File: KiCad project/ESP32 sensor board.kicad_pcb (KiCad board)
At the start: 4 copper layers, 104.8 x 50 mm, 82 parts, among them J1 USB_C_Receptacle, J2 JST_2mm_LiPo, J3 GSD090012SEU, J5 B4B-XH-AM__LF__SN_, J6 Conn_01x05, Q1 TEMT6000X01, Q2 BC817, Q3 BC817, SW1 SMD_6x3.5mm_h2.5mm, SW2 SMD_6x3.5mm_h2.5mm, U1 MCP73871, U2 AMS1117-3.3, U3 ESP32-C3-WROOM-02-H4, U4 CP2102N-A02-GQFN20, U5 USBLC6-2SC6, U6 W25Q32JVSSIQ, U7 BME280, U8 MAX4466EXK

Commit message: Replaced the button, USB, bat connector with new symbols and footprints. Completed draft layout and routing.
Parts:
- removed J5: B4B-XH-AM__LF__SN_, Project_Library:JST_B4B-XH-AM__LF__SN_
- added J4: B4B-XH-AM, Project_Library:JST_B4B-XH-AM__LF__SN_, F.Cu at (164.0, 113.8)
- C16, C18, C20: value 100n -> 0.1u
- F1: footprint Project_Library:1210 -> Fuse:Fuse_1210_3225Metric
- R4: value 5K1 -> 5k1
- SW1, SW2: value SMD_6x3.5mm_h2.5mm -> 1101NE; footprint Button_Switch_THT:SW_PUSH_6mm -> Footprints:SW4-SMD-5.2X5.2X1.5MM
- U2: value AMS1117-3.3 -> LM1117MPX-3.3_NOPB; footprint Package_TO_SOT_SMD:SOT-223-3_TabPin2 -> Footprints:VREG_LM1117MPX-3.3_NOPB
- U3: footprint Project_Library:MODULE_ESP32-C3-WROOM-02-H4 -> Footprints:MODULE_ESP32-C3-WROOM-02-H4
- U8: value MAX4466EXK -> MAX4466EXK+T
- moved SW1 4.03 mm to (197.6, 79.7), turned to 180 degrees
- moved SW2 2.88 mm to (197.5, 113.9), turned to 180 degrees
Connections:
- net /ESP32-C3-02/USB_D+ renamed Net-(U4-D+)
- net /ESP32-C3-02/USB_D- renamed Net-(U4-D-)
- SW1 pad 1: /ESP32-C3-02/BOOT -> GND
- SW2 pad 1: /ESP32-C3-02/EN -> GND
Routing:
- net GND: track 393.4 -> 244.0 mm, vias 15 -> 48
- net 3.3V: track 316.2 -> 211.5 mm, vias 17 -> 26
- net /ESP32-C3-02/BOOT: track 35.3 -> 37.8 mm, vias 1 -> 2
- net Net-(U4-~{TXT}/GPIO.2): track 23.7 -> 25.9 mm
- net /VBAT: track 18.6 -> 20.7 mm
- net Net-(U4-D-): track 14.1 -> 16.1 mm
- net Net-(U4-D+): track 22.1 -> 23.6 mm
- net /ESP32-C3-02/EN: track 45.4 -> 44.1 mm, vias 1 -> 2
- net +5V: vias 0 -> 1

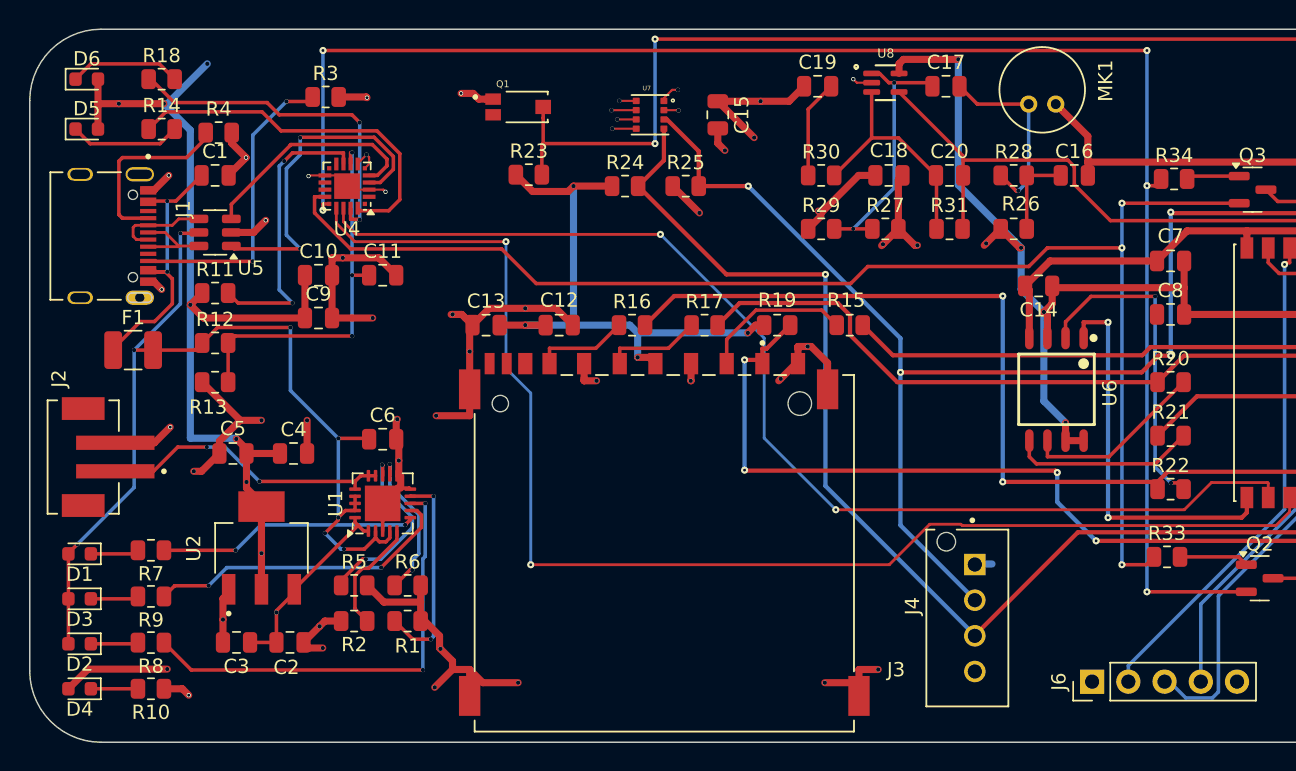
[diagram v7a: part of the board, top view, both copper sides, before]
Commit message: Replaced tantalum capacitors and LEDs.
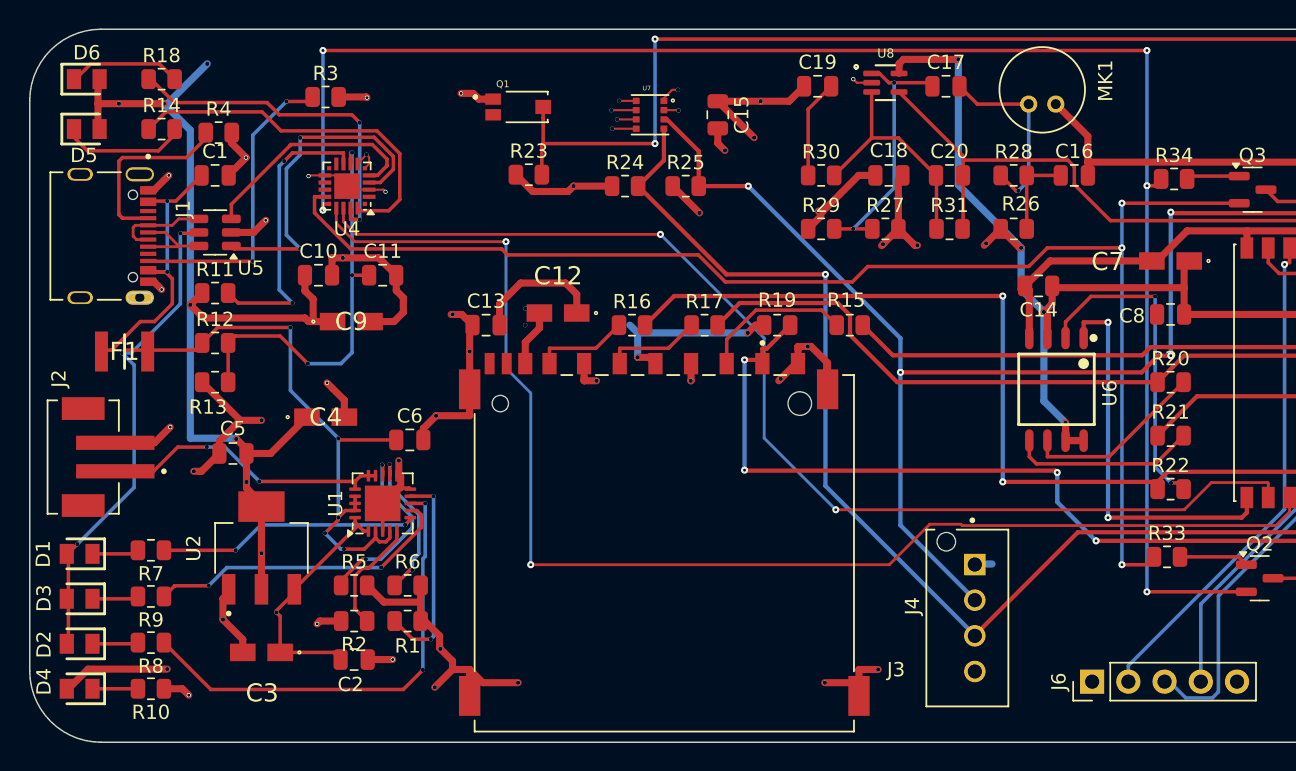
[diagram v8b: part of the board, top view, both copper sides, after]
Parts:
- C12, C3, C4, C7, C9: footprint Capacitor_SMD:C_0805_2012Metric -> Footprints:T491A
- D1, D2, D3, D4, D5, D6: footprint LED_SMD:LED_0603_1608Metric -> Footprints:LEDC2012X120N
- F1: value Polyfuse -> 0ZCH0110AF2E; footprint Fuse:Fuse_1210_3225Metric -> Footprints:FUSC3226X100N
- moved C2 4.66 mm to (121.0, 116.7)
- moved C4 3.40 mm to (119.0, 99.7)
- moved C9 2.31 mm to (120.8, 93.0)
- moved C6 1.90 mm to (124.9, 101.3)
- moved C3 1.88 mm to (114.5, 116.2)
- moved C12 0.85 mm to (135.3, 92.4)
- moved F1 0.61 mm to (104.9, 95.1)
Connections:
- C12 pad 1: GND -> 3.3V
- C12 pad 2: 3.3V -> GND
- C8 pad 1: GND -> 3.3V
- C8 pad 2: 3.3V -> GND
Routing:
- net 3.3V: track 211.5 -> 205.9 mm
- net GND: track 244.0 -> 239.2 mm, vias 48 -> 46
- net /+5V_USB: track 72.3 -> 76.5 mm
- net +5V: track 13.9 -> 17.4 mm
- net Net-(U4-VBUS): track 26.6 -> 28.9 mm
- net Net-(U1-STAT1/~{LBO}): track 31.7 -> 32.9 mm
- net Net-(D5-K): track 7.80 -> 8.84 mm
- net /VBUS: track 20.3 -> 21.0 mm
